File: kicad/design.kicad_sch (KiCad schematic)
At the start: 0 parts

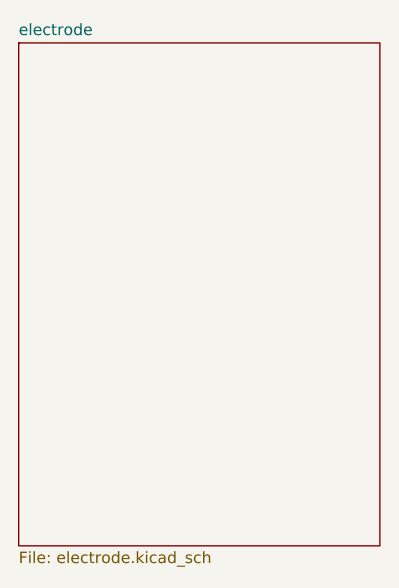
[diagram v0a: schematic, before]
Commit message: mcu changed cuz of clock requierements
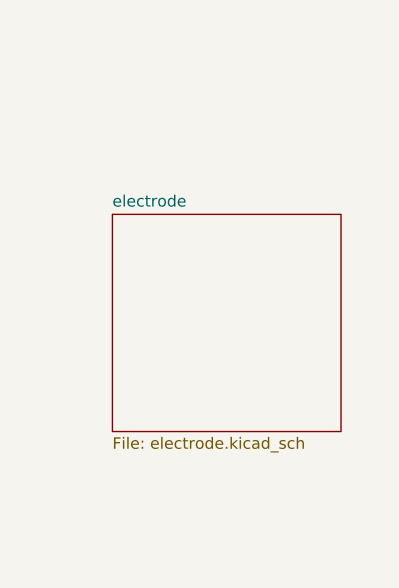
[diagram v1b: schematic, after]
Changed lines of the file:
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@@
 	(paper "A4")
 	(sheet
-		(at 114.046 69.85)
-		(size 40.132 55.88)
+		(at 124.46 88.9)
+		(size 25.4 24.13)
 		(exclude_from_sim no)
 		(in_bom yes)
@@
 		)
 		(property "Sheetname" "electrode"
-			(at 114.046 69.1384 0)
+			(at 124.46 88.1884 0)
 			(show_name no)
 			(do_not_autoplace no)
@@
 		)
 		(property "Sheetfile" "electrode.kicad_sch"
-			(at 114.046 126.3146 0)
+			(at 124.46 113.6146 0)
 			(show_name no)
 			(do_not_autoplace no)

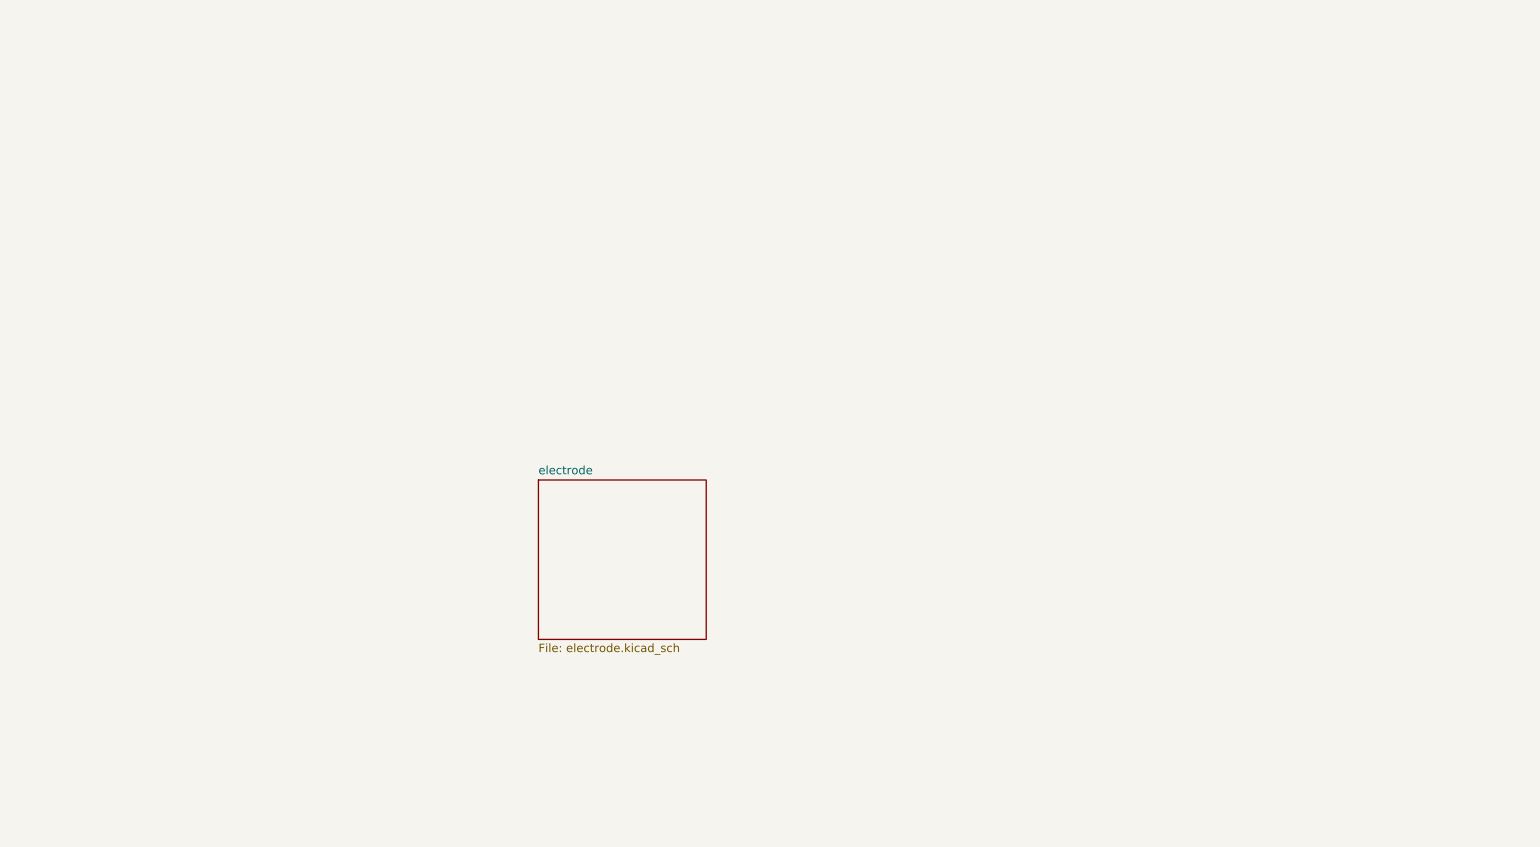
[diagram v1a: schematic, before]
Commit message: mcu chain test board with mcu side only for now
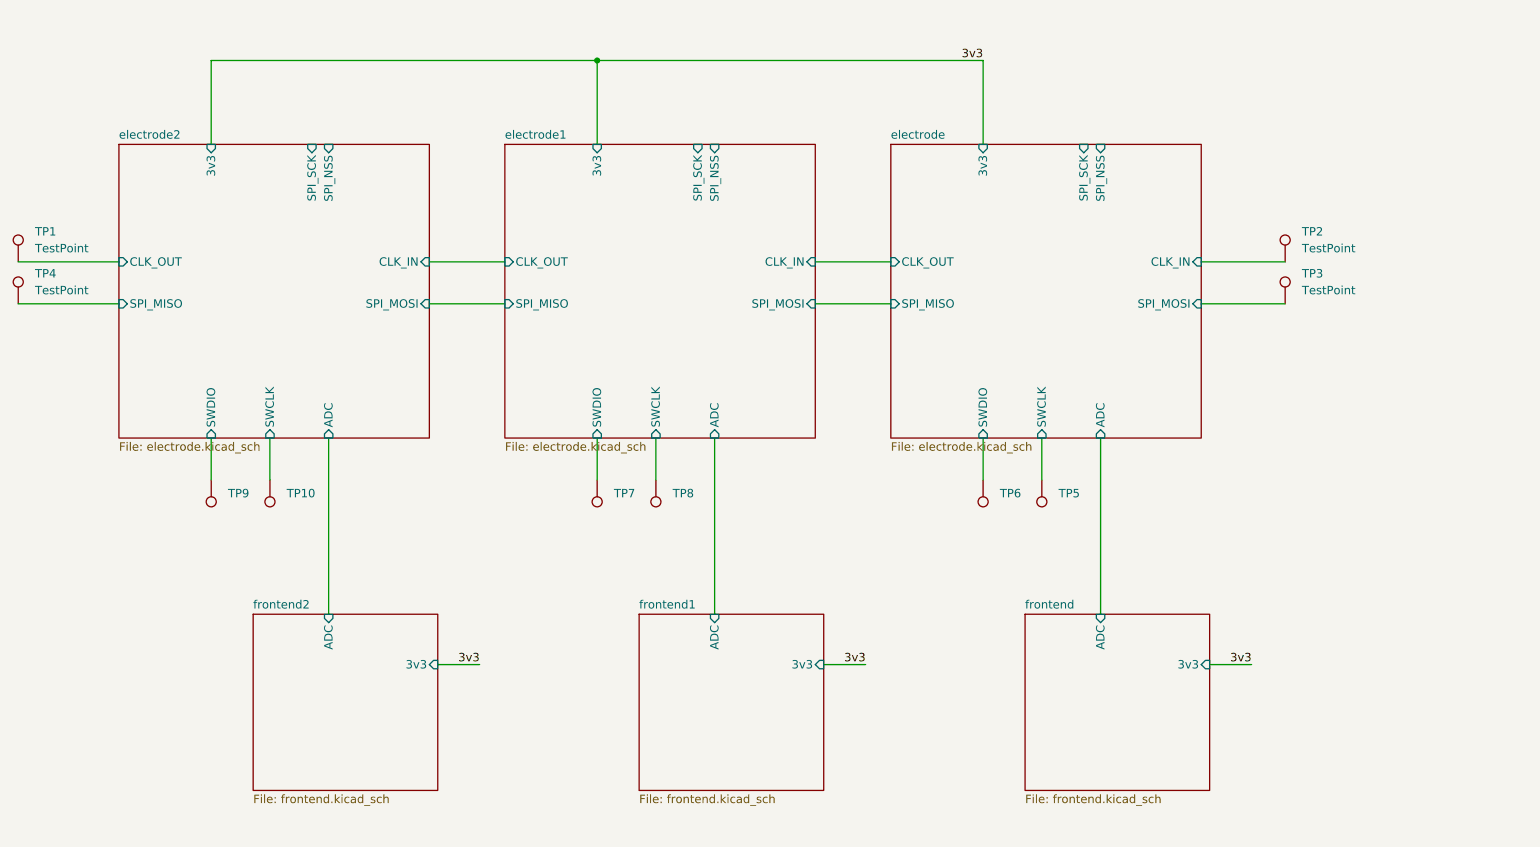
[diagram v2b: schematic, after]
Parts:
- added TP1, TP10, TP2, TP3, TP4, TP5, TP6, TP7, TP8, TP9: TestPoint, symbol Connector:TestPoint
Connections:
- new net electrode/CLK_IN: TP2.1
- new net electrode/SPI_MOSI: TP3.1
- new net electrode/SWCLK: TP5.1
- new net electrode/SWDIO: TP6.1
- new net electrode1/SWCLK: TP8.1
- new net electrode1/SWDIO: TP7.1
- new net electrode2/CLK_OUT: TP1.1
- new net electrode2/SPI_MISO: TP4.1
- new net electrode2/SWCLK: TP10.1
- new net electrode2/SWDIO: TP9.1
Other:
- added sheet electrode1 (electrode.kicad_sch)
- added sheet electrode2 (electrode.kicad_sch)
- added sheet frontend (frontend.kicad_sch)
- added sheet frontend1 (frontend.kicad_sch)
- added sheet frontend2 (frontend.kicad_sch)
- sheet electrode ports: added 3v3, ADC, CLK_IN, CLK_OUT, SPI_MISO, SPI_MOSI, SPI_NSS, SPI_SCK, SWCLK, SWDIO; removed none

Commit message: I dont remember last commit idk
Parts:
- added R1, R6, R7: 0, Resistor_SMD:R_0603_1608Metric, symbol Device:R
- added R5: 10k, Resistor_SMD:R_0603_1608Metric, symbol Device:R
- added TP14, TP15: TestPoint, TestPoint:TestPoint_Pad_2.5x2.5mm, symbol Connector:TestPoint
- TP1, TP10, TP2, TP3, TP4, TP5, TP6, TP7, TP8, TP9: footprint (none) -> TestPoint:TestPoint_Pad_2.5x2.5mm; now left out of the parts list
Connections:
- net 3v3: now also TP14.1
- net electrode/CLK_IN: now also R1.2
- net electrode/CLK_OUT: now also R6.2
- net electrode/SPI_SCK: now also R1.1
- net electrode1/CLK_OUT: now also R7.2
- net electrode1/SPI_SCK: now also R6.1
- net electrode2/SPI_SCK: now also R7.1
- new net GND: R5.2
- new net NSS: R5.1, TP15.1
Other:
- removed sheet frontend1
- removed sheet frontend2
- sheet electrode ports: added OPA_N, OPA_OUT, OPA_P; removed ADC
- sheet frontend ports: added ANALOG_IN, OPA_N, OPA_OUT, OPA_P; removed ADC
